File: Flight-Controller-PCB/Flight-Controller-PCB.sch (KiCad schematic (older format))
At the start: 29 parts, among them J1 ESC_1, J2 Receiver, J3 ESC_2, J4 ICSP, J5 ESC_3, J6 Aux, J7 ESC_4, J8 Power_In, U1 MCP6001U

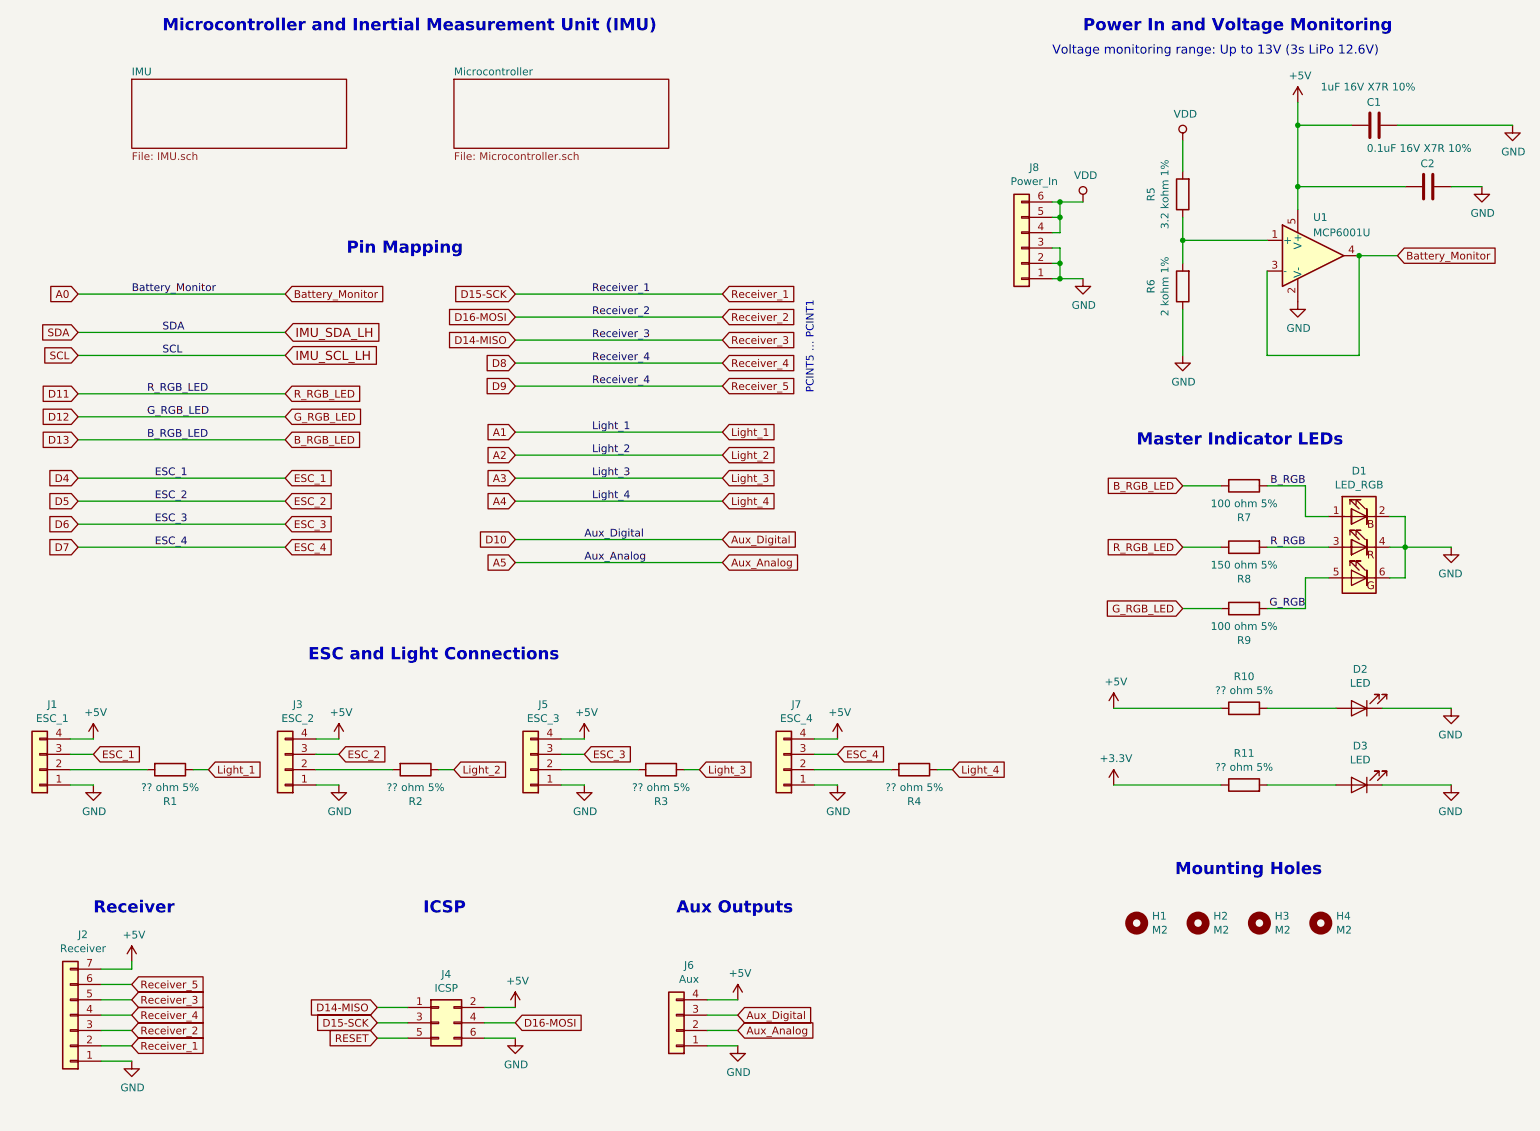
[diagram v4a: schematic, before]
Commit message: Main page and IMU reviewed and passed
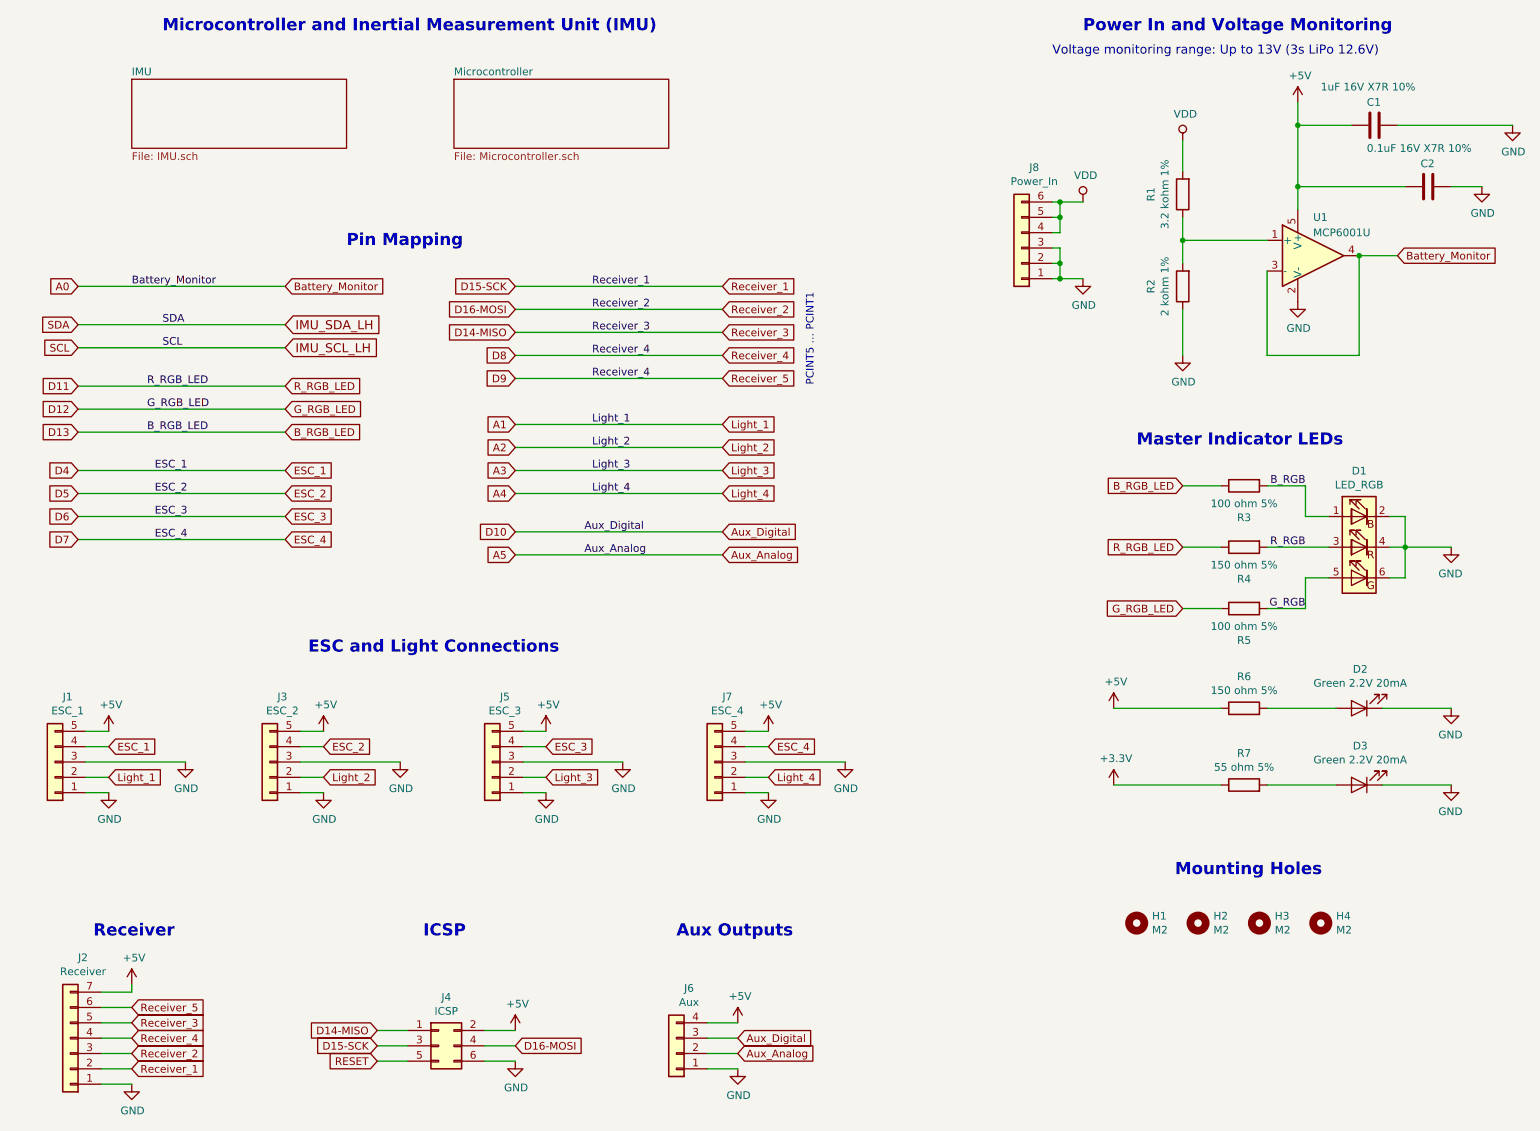
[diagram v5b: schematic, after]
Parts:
- removed J1: ESC_1, Connector_JST:JST_GH_BM04B-GHS-TBT_1x04-1MP_P1.25mm_Vertical, symbol Connector_Generic:Conn_01x04
- removed J3: ESC_2, Connector_JST:JST_GH_BM04B-GHS-TBT_1x04-1MP_P1.25mm_Vertical, symbol Connector_Generic:Conn_01x04
- removed J5: ESC_3, Connector_JST:JST_GH_BM04B-GHS-TBT_1x04-1MP_P1.25mm_Vertical, symbol Connector_Generic:Conn_01x04
- removed J7: ESC_4, Connector_JST:JST_GH_BM04B-GHS-TBT_1x04-1MP_P1.25mm_Vertical, symbol Connector_Generic:Conn_01x04
- removed R1, R2, R3, R4: ?? ohm 5%, Resistor_SMD:R_0603_1608Metric_Pad1.05x0.95mm_HandSolder, symbol Device:R
- added J1: ESC_1, Connector_JST:JST_GH_BM05B-GHS-TBT_1x05-1MP_P1.25mm_Vertical, symbol Connector_Generic:Conn_01x05
- added J3: ESC_2, Connector_JST:JST_GH_BM05B-GHS-TBT_1x05-1MP_P1.25mm_Vertical, symbol Connector_Generic:Conn_01x05
- added J5: ESC_3, Connector_JST:JST_GH_BM05B-GHS-TBT_1x05-1MP_P1.25mm_Vertical, symbol Connector_Generic:Conn_01x05
- added J7: ESC_4, Connector_JST:JST_GH_BM05B-GHS-TBT_1x05-1MP_P1.25mm_Vertical, symbol Connector_Generic:Conn_01x05
- D2, D3: value LED -> Green 2.2V 20mA
- J4: footprint (none) -> Connector_PinHeader_2.54mm:PinHeader_2x03_P2.54mm_Vertical
- R6: renamed from R10; value ?? ohm 5% -> 150 ohm 5%
- R7: renamed from R11; value ?? ohm 5% -> 55 ohm 5%
- renumbered R5 to R1, R6 to R2, R7 to R3, R8 to R4, R9 to R5
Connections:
- net +5V: now also J1.5 (Pin_5), J3.5 (Pin_5), J5.5 (Pin_5), J7.5 (Pin_5)
- net A1: now also J1.2 (Pin_2)
- net A2: now also J3.2 (Pin_2)
- net A3: now also J5.2 (Pin_2)
- net A4: now also J7.2 (Pin_2)
- net D4: now also J1.4 (Pin_4)
- net D5: now also J3.4 (Pin_4)
- net D6: now also J5.4 (Pin_4)
- net D7: now also J7.4 (Pin_4)
- net GND: now also J1.1 (Pin_1), J1.3 (Pin_3), J3.1 (Pin_1), J3.3 (Pin_3), J5.1 (Pin_1), J5.3 (Pin_3), J7.1 (Pin_1), J7.3 (Pin_3)
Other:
- moved on the sheet: J2, J4, J6

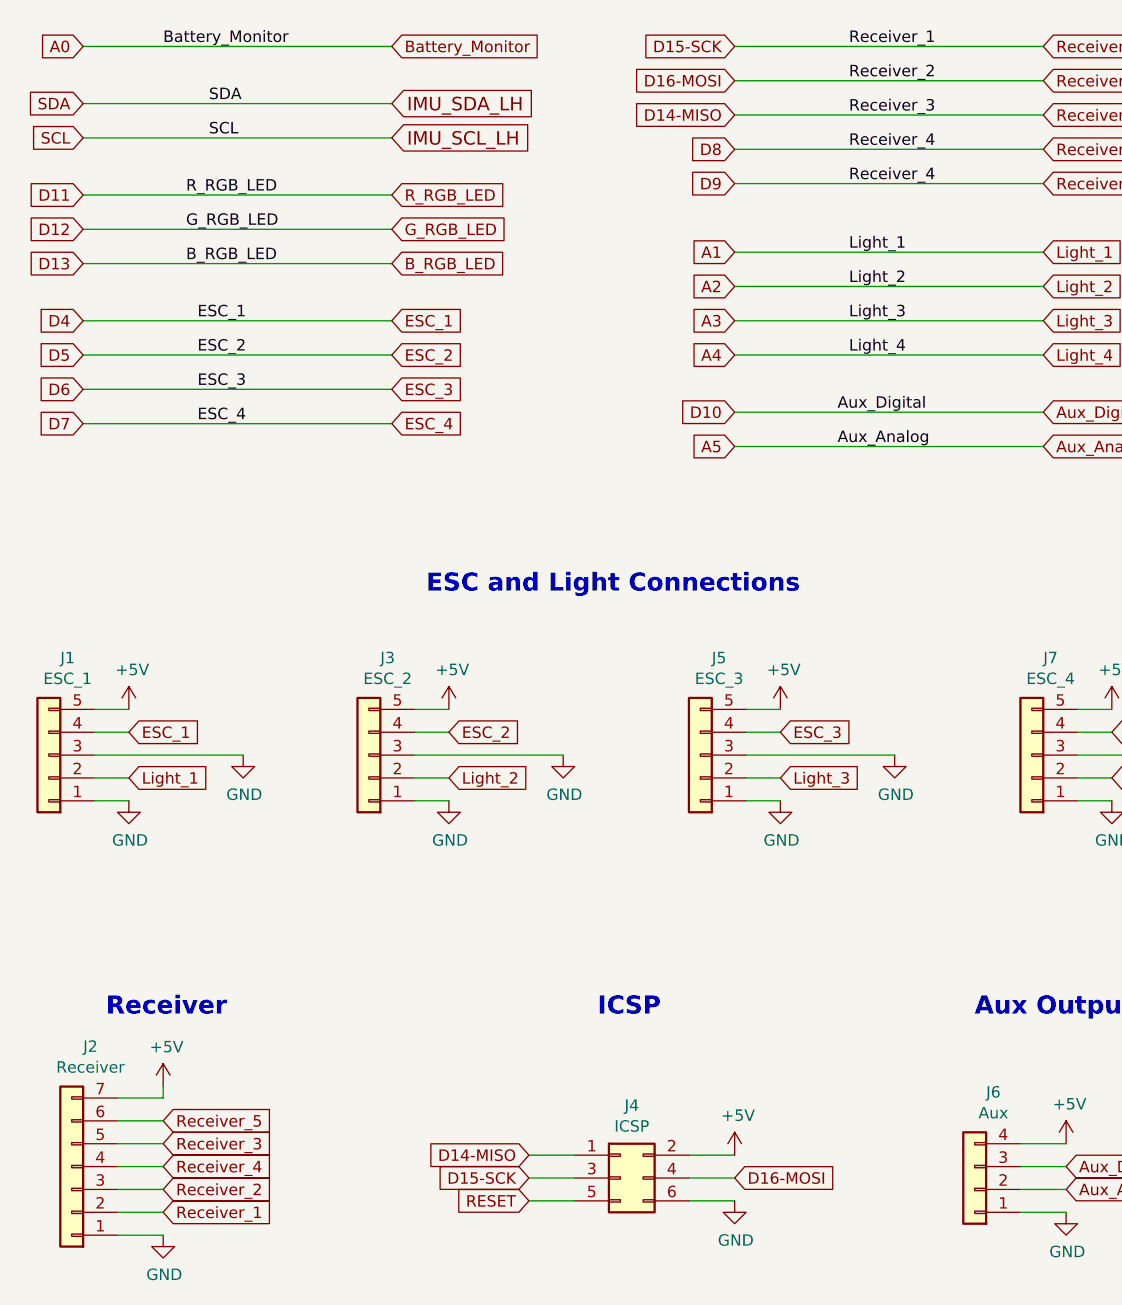
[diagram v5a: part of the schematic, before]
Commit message: Placed the crystal and IMU is mostly routed
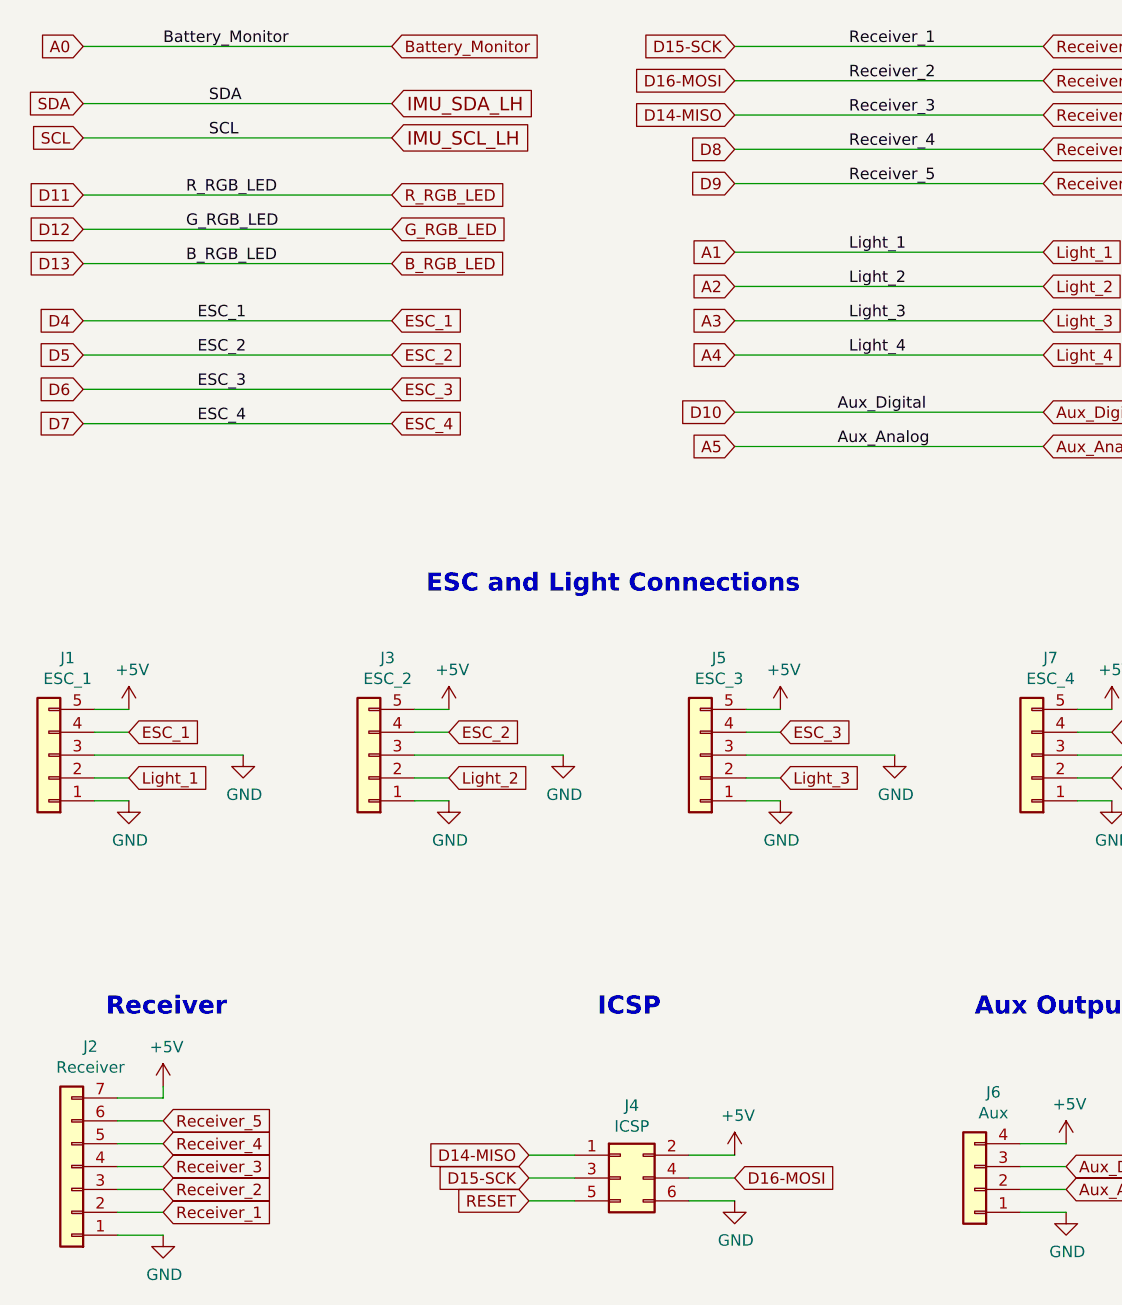
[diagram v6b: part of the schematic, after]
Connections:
- net D14-MISO: now also J2.4 (Pin_4); no longer J2.5 (Pin_5)
- net D8: now also J2.5 (Pin_5); no longer J2.4 (Pin_4), J2.6 (Pin_6)
- new net D9: J2.6 (Pin_6)
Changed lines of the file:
@@
 Text GLabel 1350 7400 2    50   Input ~ 0
 Receiver_2
+Text GLabel 1350 7300 2    50   Input ~ 0
+Receiver_3
 Text GLabel 1350 7200 2    50   Input ~ 0
-Receiver_3
-Text GLabel 1350 7300 2    50   Input ~ 0
 Receiver_4
 $Comp
@@
 	1150 7400 1350 7400
 Wire Wire Line
-	1350 7200 1150 7200
+	1350 7300 1150 7300
 Wire Wire Line
-	1150 7300 1350 7300
+	1150 7200 1350 7200
 Wire Wire Line
 	7350 2250 7400 2250
@@
 	5200 3000 3850 3000
 Text Label 4350 3000 0    50   ~ 0
-Receiver_4
+Receiver_5
 Text GLabel 1350 7100 2    50   Input ~ 0
 Receiver_5
